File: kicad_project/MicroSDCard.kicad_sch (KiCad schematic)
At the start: 6 parts, among them J8 DM3AT, U13 74LVC1G125

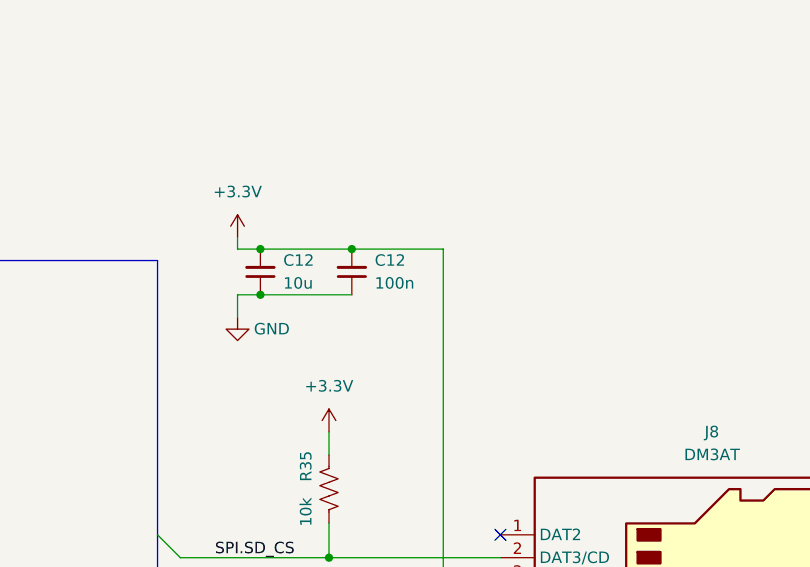
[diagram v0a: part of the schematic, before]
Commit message: Add part numbers for capacitors, start working on BoM job
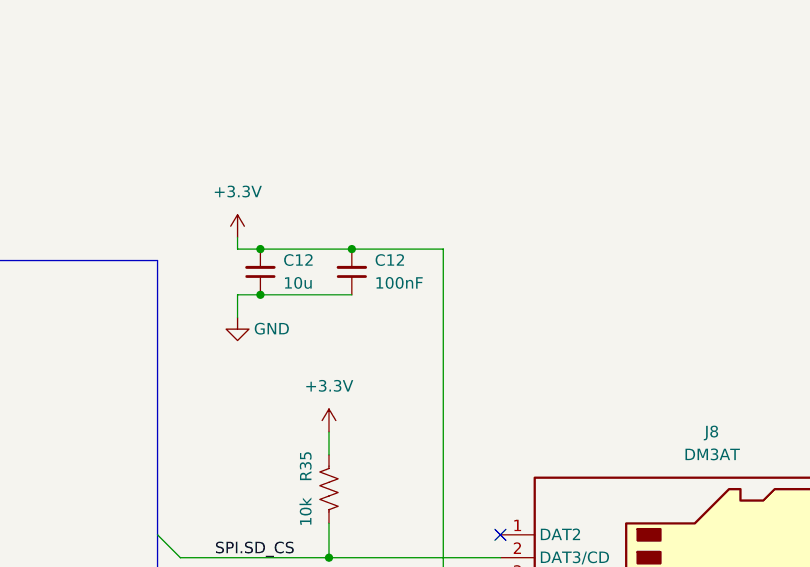
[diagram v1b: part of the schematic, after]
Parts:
- C12: LibRef (none) -> CL31B106KLHNNNE; Supplier (none) -> Digi-Key
- C12: value 100n -> 100nF; LibRef (none) -> GRM319R72A104KA01D; Supplier (none) -> Digi-Key
- J8, R35, U13: Supplier (none) -> Digi-Key
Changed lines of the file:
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@@
+      (effects (font (size 1.27 1.27)) hide)
+    )
+    (property "Supplier" "Digi-Key" (at 69.85 88.9 0)
+      (effects (font (size 1.27 1.27)) hide)
+    )
+    (property "LibRef" "" (at 69.85 88.9 0)
       (effects (font (size 1.27 1.27)) hide)
     )
@@
       (effects (font (size 1.27 1.27)) hide)
     )
+    (property "Supplier" "Digi-Key" (at 67.31 113.03 0)
+      (effects (font (size 1.27 1.27)) hide)
+    )
+    (property "LibRef" "" (at 67.31 113.03 0)
+      (effects (font (size 1.27 1.27)) hide)
+    )
     (pin "1")
     (pin "2")
@@
     )
     (property "SKU" "HR1964CT-ND" (at 173.99 93.98 0)
+      (effects (font (size 1.27 1.27)) hide)
+    )
+    (property "Supplier" "Digi-Key" (at 173.99 93.98 0)
+      (effects (font (size 1.27 1.27)) hide)
+    )
+    (property "LibRef" "" (at 173.99 93.98 0)
       (effects (font (size 1.27 1.27)) hide)
     )
@@
       (effects (font (size 1.27 1.27)) hide)
     )
+    (property "Supplier" "Digi-Key" (at 132.08 78.74 0)
+      (effects (font (size 1.27 1.27)) hide)
+    )
+    (property "LibRef" "" (at 132.08 78.74 0)
+      (effects (font (size 1.27 1.27)) hide)
+    )
     (pin "1")
     (pin "2")
@@
       (effects (font (size 1.27 1.27)) hide)
     )
+    (property "Supplier" "Digi-Key" (at 124.46 54.61 0)
+      (effects (font (size 1.27 1.27)) hide)
+    )
+    (property "LibRef" "CL31B106KLHNNNE" (at 124.46 54.61 0)
+      (effects (font (size 1.27 1.27)) hide)
+    )
     (pin "1")
     (pin "2")
@@
       (effects (font (size 1.27 1.27)) (justify right))
     )
-    (property "Value" "100n" (at 137.16 55.8736 0)
+    (property "Value" "100nF" (at 137.16 55.8736 0)
       (effects (font (size 1.27 1.27)) (justify right))
     )
@@
       (effects (font (size 1.27 1.27)) hide)
     )
+    (property "SKU" "" (at 134.62 54.61 0)
+      (effects (font (size 1.27 1.27)) hide)
+    )
+    (property "Supplier" "Digi-Key" (at 134.62 54.61 0)
+      (effects (font (size 1.27 1.27)) hide)
+    )
+    (property "LibRef" "GRM319R72A104KA01D" (at 134.62 54.61 0)
+      (effects (font (size 1.27 1.27)) hide)
+    )

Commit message: Fill in all part numbers, add pcbinv bom job
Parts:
- R35: LibRef (none) -> ERJ-8ENF1002V; SKU (none) -> P10.0KFCT-ND
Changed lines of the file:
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@@
       (effects (font (size 1.27 1.27)) hide)
     )
-    (property "LibRef" "" (at 132.08 78.74 0)
+    (property "LibRef" "ERJ-8ENF1002V" (at 132.08 78.74 0)
       (effects (font (size 1.27 1.27)) hide)
     )
+    (property "SKU" "P10.0KFCT-ND" (at 132.08 78.74 0)
+      (effects (font (size 1.27 1.27)) hide)
+    )

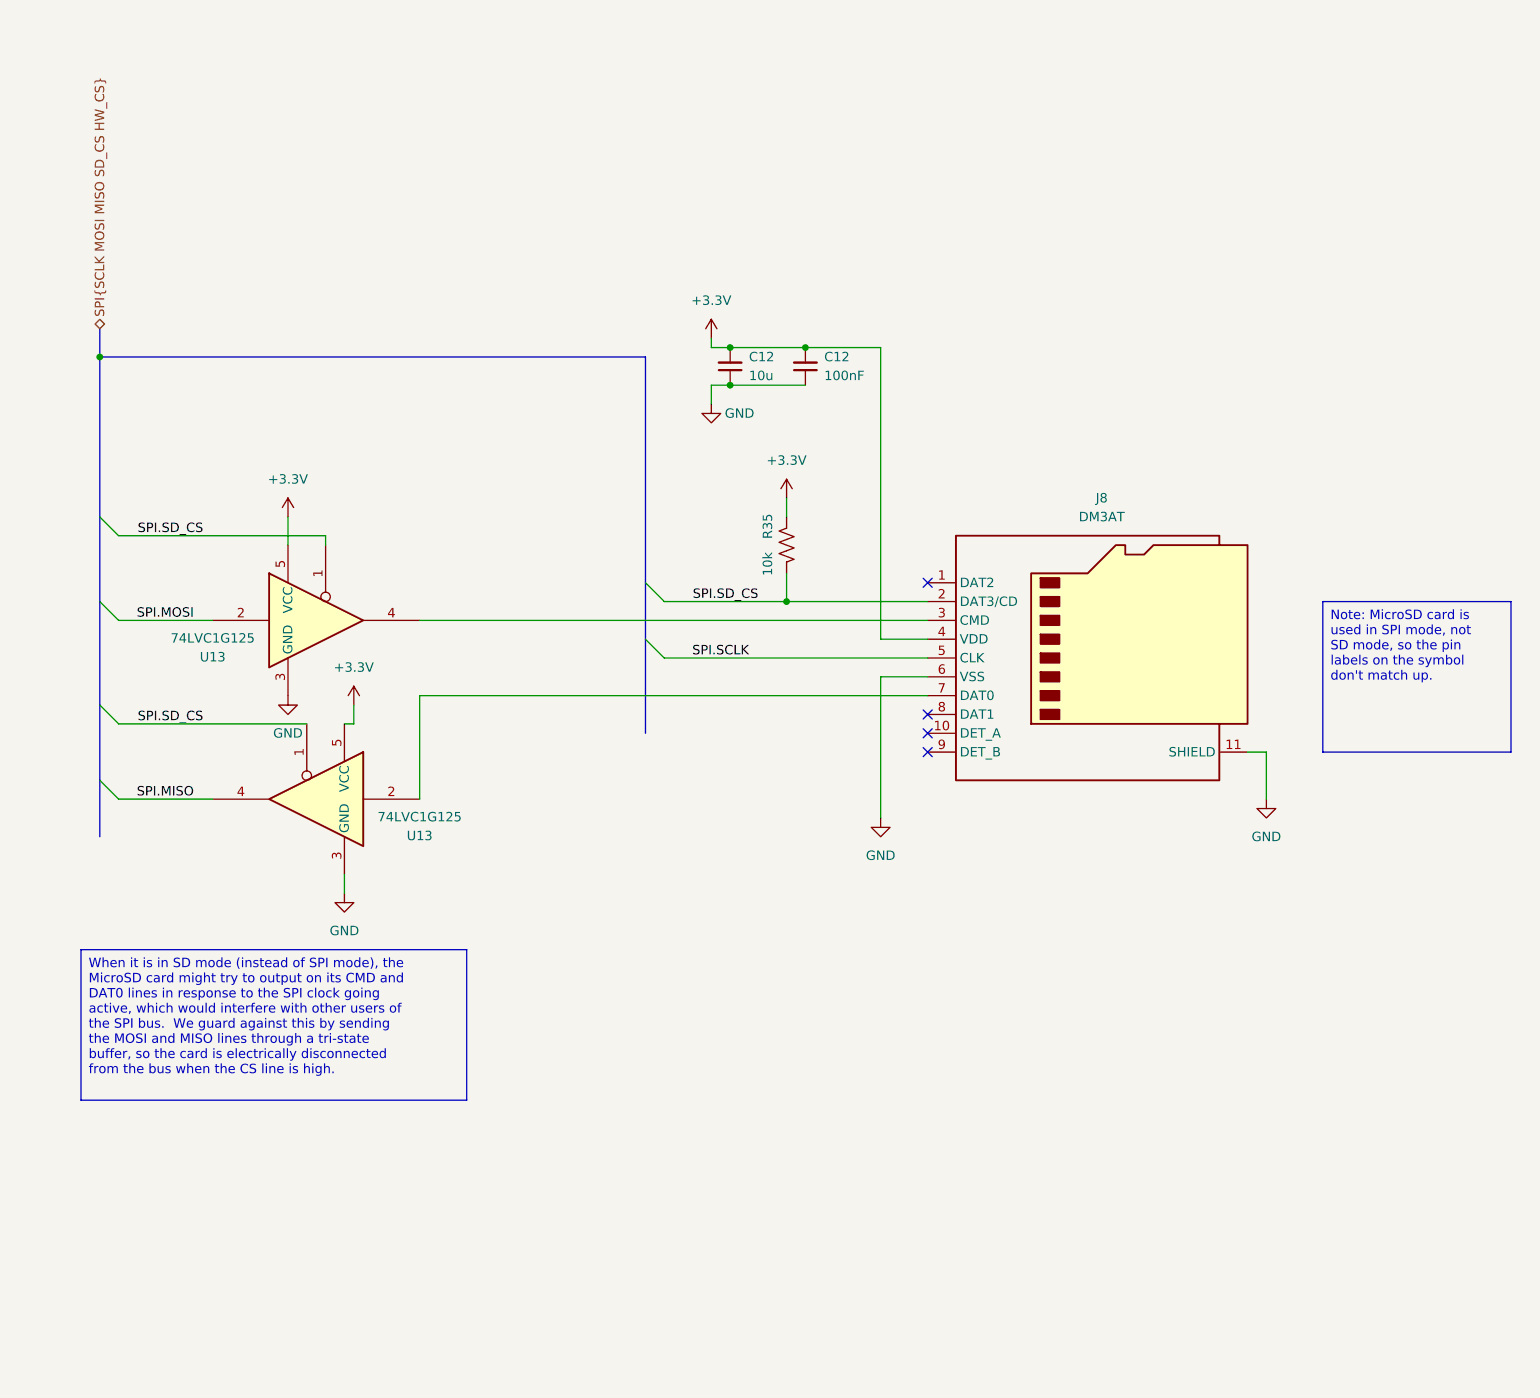
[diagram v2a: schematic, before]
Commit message: Add diode on SD card CS line, fix position of PWM/analog testing capacitor
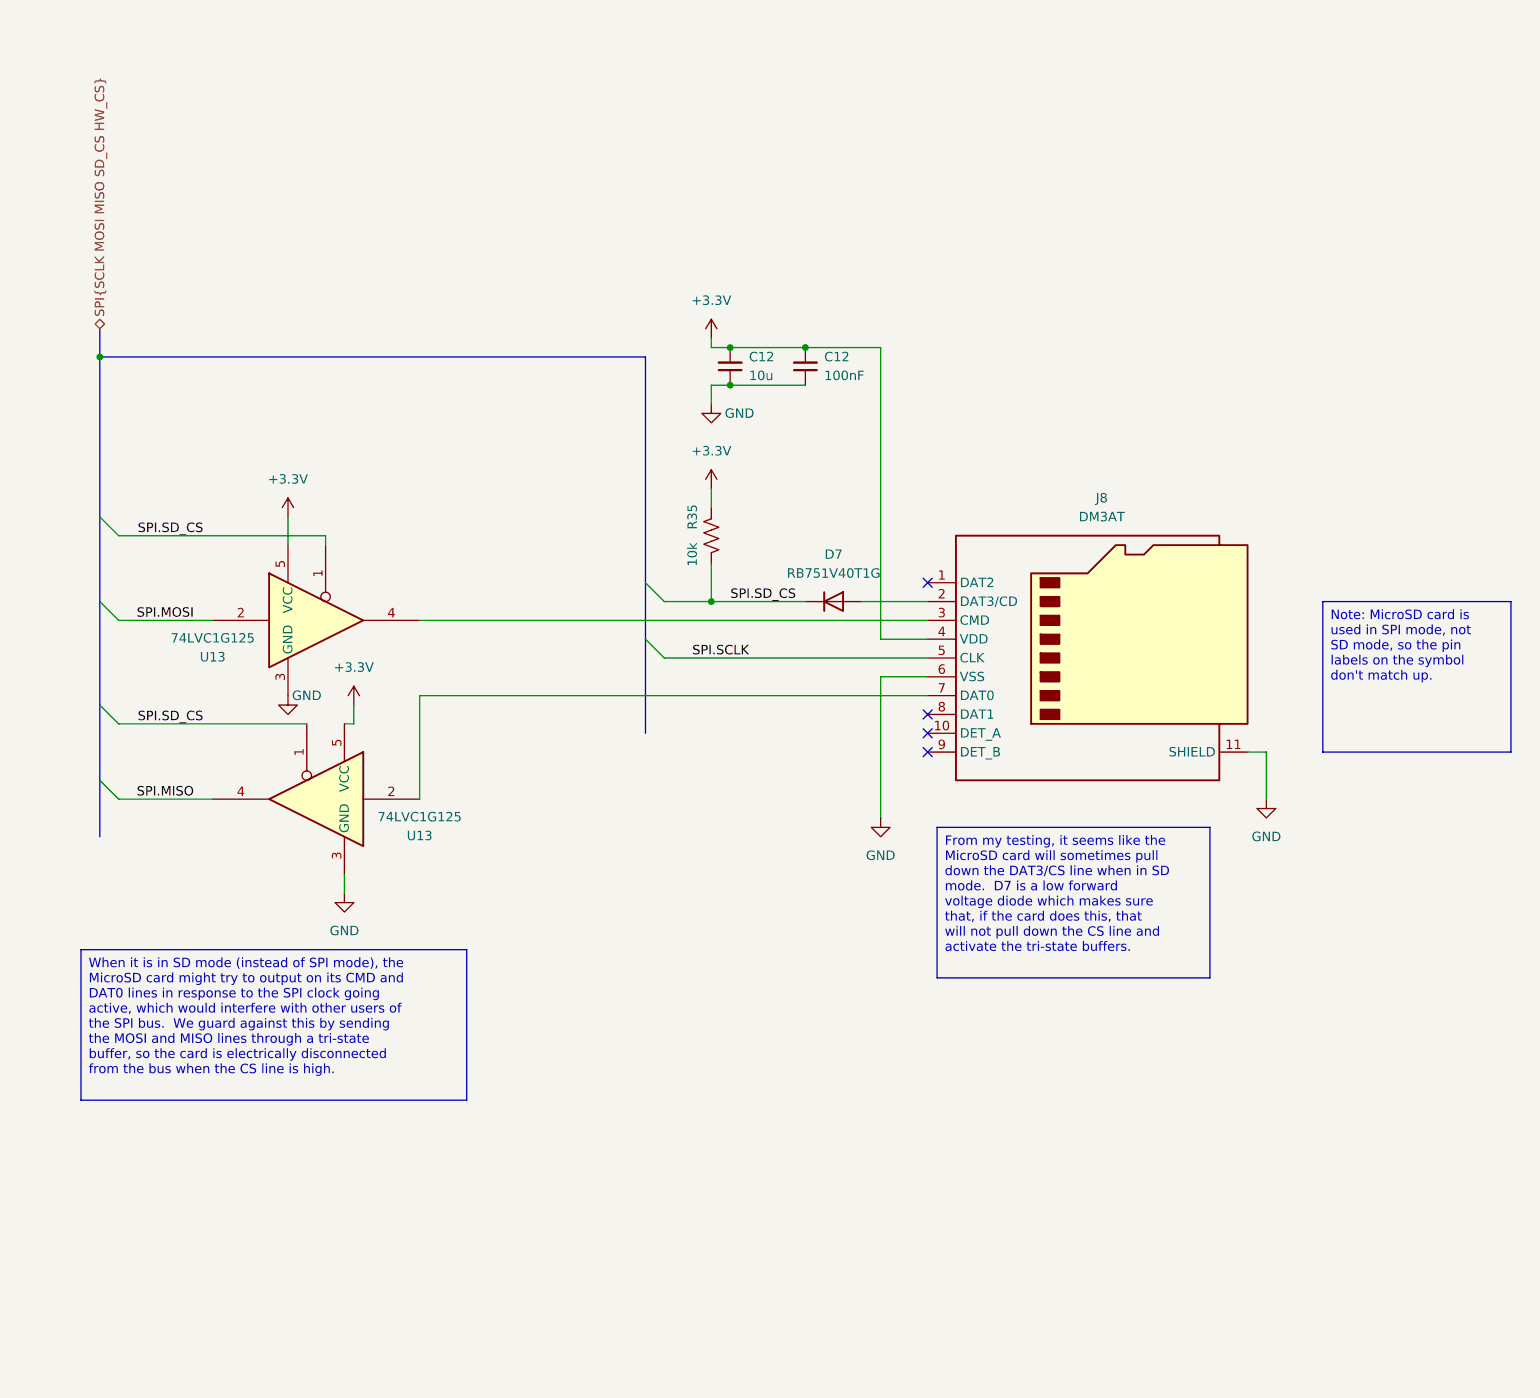
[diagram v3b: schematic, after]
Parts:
- added D7: RB751V40T1G, Diode_SMD:D_SOD-323, symbol project libraries:RB751V40T1G
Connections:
- net SPI.SD_CS: now also D7.1 (K); no longer J8.2 (DAT3/CD)
- new net: D7.2 (A), J8.2 (DAT3/CD)
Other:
- moved on the sheet: R35
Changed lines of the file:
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@@
   (junction (at 39.37 53.34) (diameter 0) (color 0 0 0 0)
   )
-  (junction (at 132.08 86.36) (diameter 0) (color 0 0 0 0)
-  )
   (junction (at 124.46 52.07) (diameter 0) (color 0 0 0 0)
+  )
+  (junction (at 121.92 86.36) (diameter 0) (color 0 0 0 0)
   )
   (junction (at 124.46 57.15) (diameter 0) (color 0 0 0 0)
@@
     (stroke (width 0) (type default))
   )
-  (wire (pts (xy 115.57 86.36) (xy 132.08 86.36))
+  (wire (pts (xy 115.57 86.36) (xy 121.92 86.36))
     (stroke (width 0) (type default))
   )
@@
     (stroke (width 0) (type default))
   )
+  (wire (pts (xy 121.92 86.36) (xy 134.62 86.36))
+    (stroke (width 0) (type default))
+  )
   (bus (pts (xy 113.03 53.34) (xy 113.03 83.82))
     (stroke (width 0) (type default))
@@
     (stroke (width 0) (type default))
   )
-  (wire (pts (xy 132.08 82.55) (xy 132.08 86.36))
+  (wire (pts (xy 121.92 81.28) (xy 121.92 86.36))
     (stroke (width 0) (type default))
   )
@@
     (stroke (width 0) (type default))
   )
-  (wire (pts (xy 132.08 72.39) (xy 132.08 74.93))
+  (wire (pts (xy 121.92 71.12) (xy 121.92 73.66))
     (stroke (width 0) (type default))
   )
@@
     (stroke (width 0) (type default))
   )
-  (wire (pts (xy 132.08 86.36) (xy 151.13 86.36))
-    (stroke (width 0) (type default))
-  )
   (wire (pts (xy 64.77 74.93) (xy 64.77 78.74))
     (stroke (width 0) (type default))
@@
   )
   (wire (pts (xy 124.46 52.07) (xy 134.62 52.07))
+    (stroke (width 0) (type default))
+  )
+  (wire (pts (xy 142.24 86.36) (xy 151.13 86.36))
     (stroke (width 0) (type default))
   )
@@
     (effects (font (size 1.27 1.27)) (justify left top))
   )
+  (text_box "From my testing, it seems like the MicroSD card will sometimes pull down the DAT3/CS line when in SD mode.  D7 is a low forward voltage diode which makes sure that, if the card does this, that will not pull down the CS line and activate the tri-state buffers."
+    (at 152.4 116.84 0) (size 36.83 20.32)
+    (stroke (width 0) (type default))
+    (fill (type none))
+    (effects (font (size 1.27 1.27)) (justify left top))
+  )
   (text_box "When it is in SD mode (instead of SPI mode), the MicroSD card might try to output on its CMD and DAT0 lines in response to the SPI clock going active, which would interfere with other users of the SPI bus.  We guard against this by sending the MOSI and MISO lines through a tri-state buffer, so the card is electrically disconnected from the bus when the CS line is high."
     (at 36.83 133.35 0) (size 52.07 20.32)
@@
     (effects (font (size 1.27 1.27)) (justify right bottom))
   )
-  (label "SPI.SD_CS" (at 128.27 86.36 180) (fields_autoplaced)
+  (label "SPI.SD_CS" (at 133.35 86.36 180) (fields_autoplaced)
     (effects (font (size 1.27 1.27)) (justify right bottom))
   )
@@
     )
   )
-  (symbol (lib_id "power:+3.3V") (at 132.08 72.39 0) (unit 1)
-    (in_bom yes) (on_board yes) (dnp no) (fields_autoplaced)
-    (property "Reference" "#PWR019" (at 132.08 76.2 0)
-      (effects (font (size 1.27 1.27)) hide)
-    )
-    (property "Value" "+3.3V" (at 132.08 67.31 0)
-      (effects (font (size 1.27 1.27)))
-    )
-    (property "Footprint" "" (at 132.08 72.39 0)
-      (effects (font (size 1.27 1.27)) hide)
-    )
-    (property "Datasheet" "" (at 132.08 72.39 0)
+  (symbol (lib_id "power:+3.3V") (at 121.92 71.12 0) (unit 1)
+    (in_bom yes) (on_board yes) (dnp no) (fields_autoplaced)
+    (property "Reference" "#PWR019" (at 121.92 74.93 0)
+      (effects (font (size 1.27 1.27)) hide)
+    )
+    (property "Value" "+3.3V" (at 121.92 66.04 0)
+      (effects (font (size 1.27 1.27)))
+    )
+    (property "Footprint" "" (at 121.92 71.12 0)
+      (effects (font (size 1.27 1.27)) hide)
+    )
+    (property "Datasheet" "" (at 121.92 71.12 0)
       (effects (font (size 1.27 1.27)) hide)
     )
@@
   )
   (symbol (lib_id "power:GND") (at 64.77 99.06 0) (unit 1)
-    (in_bom yes) (on_board yes) (dnp no) (fields_autoplaced)
+    (in_bom yes) (on_board yes) (dnp no)
     (property "Reference" "#PWR068" (at 64.77 105.41 0)
       (effects (font (size 1.27 1.27)) hide)
     )
-    (property "Value" "GND" (at 64.77 104.14 0)
+    (property "Value" "GND" (at 67.31 99.06 0)
       (effects (font (size 1.27 1.27)))
     )
@@
     )
   )
-  (symbol (lib_id "Device:R_US") (at 132.08 78.74 0) (mirror x) (unit 1)
+  (symbol (lib_id "Device:R_US") (at 121.92 77.47 0) (mirror x) (unit 1)
     (in_bom yes) (on_board yes) (dnp no)
-    (property "Reference" "R35" (at 129.54 76.2 90)
-      (effects (font (size 1.27 1.27)))
-    )
-    (property "Value" "10k" (at 129.54 81.28 90)
-      (effects (font (size 1.27 1.27)))
-    )
-    (property "Footprint" "Resistor_SMD:R_1206_3216Metric" (at 133.096 78.486 90)
-      (effects (font (size 1.27 1.27)) hide)
-    )
-    (property "Datasheet" "~" (at 132.08 78.74 0)
-      (effects (font (size 1.27 1.27)) hide)
-    )
-    (property "Supplier" "Digi-Key" (at 132.08 78.74 0)
-      (effects (font (size 1.27 1.27)) hide)
-    )
-    (property "LibRef" "ERJ-8ENF1002V" (at 132.08 78.74 0)
-      (effects (font (size 1.27 1.27)) hide)
-    )
-    (property "SKU" "P10.0KFCT-ND" (at 132.08 78.74 0)
+    (property "Reference" "R35" (at 119.38 74.93 90)
+      (effects (font (size 1.27 1.27)))
+    )
+    (property "Value" "10k" (at 119.38 80.01 90)
+      (effects (font (size 1.27 1.27)))
+    )
+    (property "Footprint" "Resistor_SMD:R_1206_3216Metric" (at 122.936 77.216 90)
+      (effects (font (size 1.27 1.27)) hide)
+    )
+    (property "Datasheet" "~" (at 121.92 77.47 0)
+      (effects (font (size 1.27 1.27)) hide)
+    )
+    (property "Supplier" "Digi-Key" (at 121.92 77.47 0)
+      (effects (font (size 1.27 1.27)) hide)
+    )
+    (property "LibRef" "ERJ-8ENF1002V" (at 121.92 77.47 0)
+      (effects (font (size 1.27 1.27)) hide)
+    )
+    (property "SKU" "P10.0KFCT-ND" (at 121.92 77.47 0)
       (effects (font (size 1.27 1.27)) hide)
     )
@@
         )
       )
+    )
+  )
+  (symbol (lib_id "project libraries:RB751V40T1G") (at 138.43 86.36 0) (unit 1)
+    (in_bom yes) (on_board yes) (dnp no) (fields_autoplaced)
+    (property "Reference" "D7" (at 138.43 80.01 0)
+      (effects (font (size 1.27 1.27)))
+    )
+    (property "Value" "RB751V40T1G" (at 138.43 82.55 0)
+      (effects (font (size 1.27 1.27)))
+    )
+    (property "Footprint" "Diode_SMD:D_SOD-323" (at 138.43 90.805 0)
+      (effects (font (size 1.27 1.27)) hide)
+    )
+    (property "Datasheet" "https://www.onsemi.com/pdf/datasheet/rb751v40t1-d.pdf" (at 138.43 92.71 0)
+      (effects (font (size 1.27 1.27)) hide)
+    )
+    (property "Sim.Device" "D" (at 138.43 97.79 0)
+      (effects (font (size 1.27 1.27)) hide)
+    )
+    (property "Sim.Pins" "1=K 2=A" (at 138.43 95.25 0)
+      (effects (font (size 1.27 1.27)) hide)
+    )
+    (property "Supplier" "Digi-Key" (at 138.43 100.33 0)
+      (effects (font (size 1.27 1.27)) hide)
+    )
+    (property "SKU" "RB751V40T1GOSCT-ND" (at 139.7 102.87 0)
+      (effects (font (size 1.27 1.27)) hide)
+    )
+    (pin "1")
+    (pin "2")
+    (instances
+      (project "mbed-ce-ci-shield-v2"
+        (path "/a0f40274-9469-4bcf-885c-e8b8a490ea54/25f8559c-e7f1-47b3-be11-aaa166453322"
+          (reference "D7") (unit 1)
+        )
+      )
